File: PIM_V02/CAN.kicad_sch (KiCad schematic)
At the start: 40 parts, among them U4 MCP2562FDT-E/SN, U5 MCP2562FDT-E/SN

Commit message: more changes, near final schematic and part way through layout now
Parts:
- removed FL1, FL2: ACT45B-101-2P-TL003, CustomFootprints:ACT45B-101-2P-TL003_TDK, symbol Custom_Components:ACT45B-101-2P-TL003
- added FL1, FL2: Choke_CommonMode_FerriteCore_1243, Inductor_SMD:L_CommonModeChoke_Coilcraft_1812CAN, symbol Filter:Choke_CommonMode_FerriteCore_1243
- C10, C11, C14, C15: value C_Small -> 4.7uF
- C12, C13, C16, C17: value C_Small -> 0.1uF
- C18, C19, C20, C21, C22, C23, C24, C25: value C_Small -> 47pF
- C26, C27: value C_Small -> 4.7nF
- R14, R15: value R_Small -> 10kR
- R16, R17: value R_Small -> 0R
- R18, R19, R20, R21: value R_Small -> 60R
- R41, R42, R43, R44: value R_Small -> 1kR
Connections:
- net CAN0_N: now also FL1.2
- net CAN0_P: now also FL1.3
- net CAN0_RAW_N: now also FL1.1
- net CAN0_RAW_P: now also FL1.4
- net CAN1_N: now also FL2.2
- net CAN1_P: now also FL2.3
- net CAN1_RAW_N: now also FL2.1
- net CAN1_RAW_P: now also FL2.4
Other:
- note removed: "Common Mode Choke: - ACT1210L-101-2P-TL00 - If HF noise hits both lines in same dir, mag fields add together, creating high imepdance wall, suffocating noise"
- note removed: "PCHAN: LOGIC LEVEL 5V AO3401 or DMP2305"
- note removed: "READ THIS https://www.onsemi.com/download/application-notes/pdf/and90146-d.pdf"
- note removed: "TVS Diode: - VCAN16A2-03S-E3-08"
- note removed: "bus-line caps should be C0G/NP0 (X7R loses capacitance with applied voltage and is microphonic, so it distorts CAN edges nonlinearly)"
- note removed: "choke dot polarity??"
- note removed: "redundant can can high and low and gnd on 3 pin header AND HEADER"
- moved on the sheet: C10, C11, C12, C13, C14, C15, C16, C17, C18, C19, C20, C21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

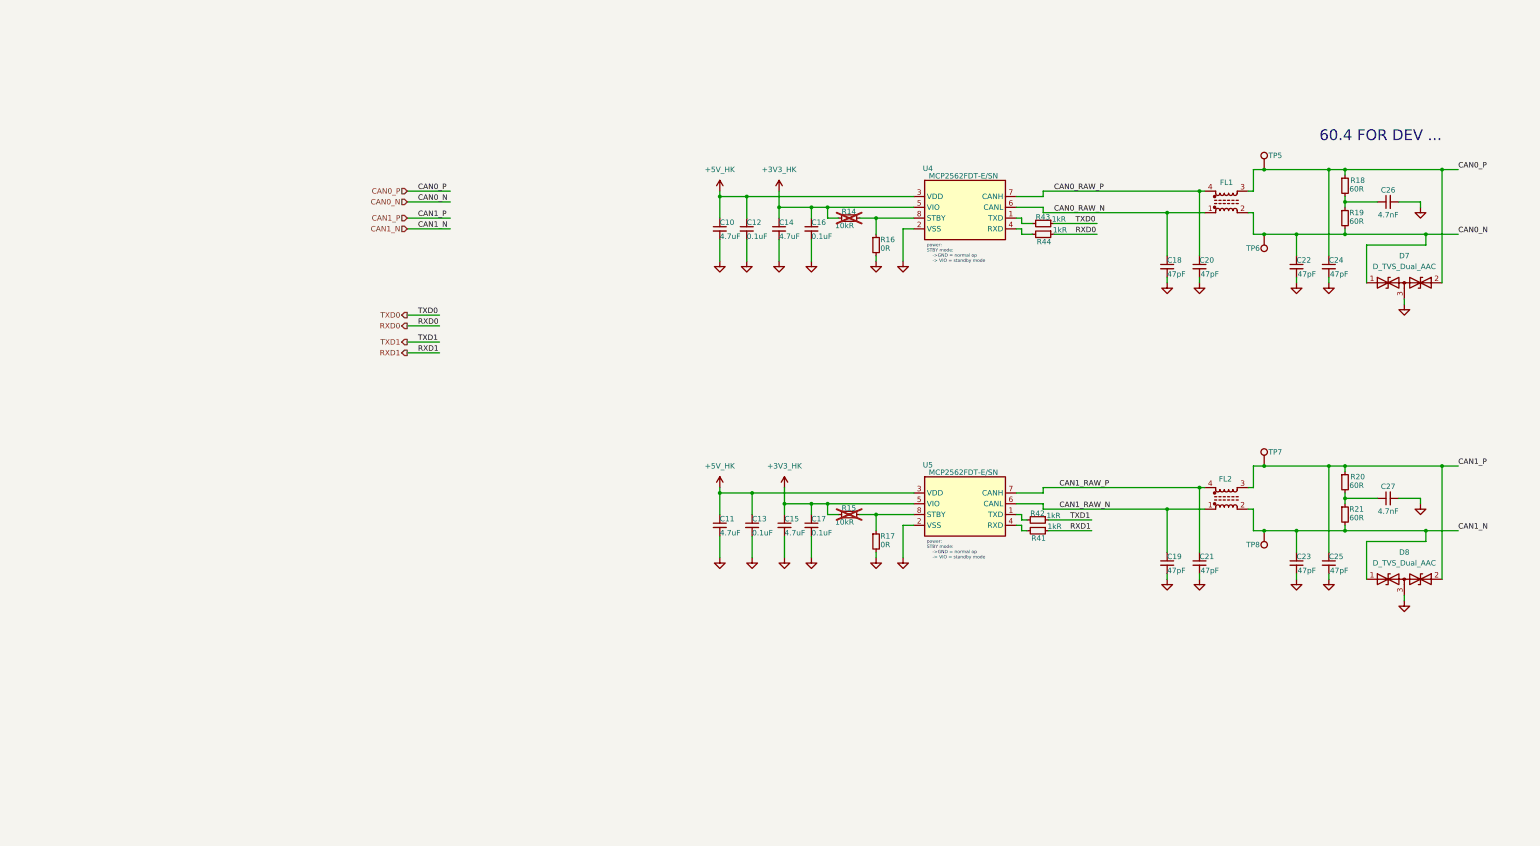
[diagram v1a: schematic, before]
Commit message: pc104 outline, nearly done with layout, managed to keep it at 4 layers but the traces became quite messy; still need to do an in depth review to ensure i havent cut across any zones unknowingly; also there are still DRC errors that i need to work through - but all nets are connected !
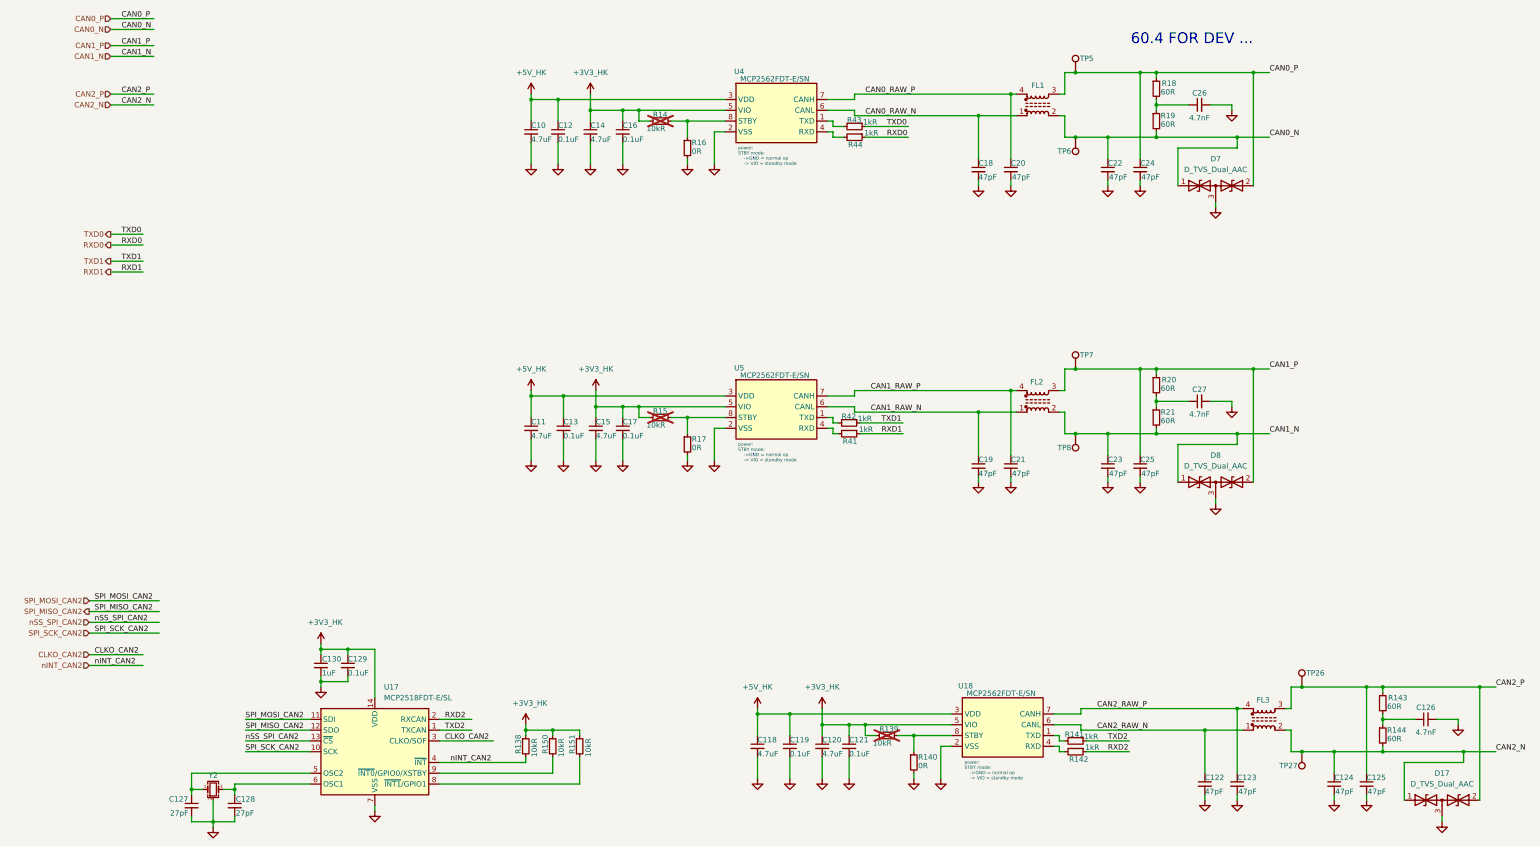
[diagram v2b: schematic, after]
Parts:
- added C118, C120: 4.7uF, Capacitor_SMD:C_0603_1608Metric, symbol Device:C_Small
- added C119, C121, C129: 0.1uF, Capacitor_SMD:C_0603_1608Metric, symbol Device:C_Small
- added C122, C123, C124, C125: 47pF, Capacitor_SMD:C_0603_1608Metric, symbol Device:C_Small
- added C126: 4.7nF, Capacitor_SMD:C_0603_1608Metric, symbol Device:C_Small
- added C127, C128: 27pF, Capacitor_SMD:C_0603_1608Metric, symbol Device:C_Small
- added C130: 1uF, Capacitor_SMD:C_0603_1608Metric, symbol Device:C_Small
- added D17: D_TVS_Dual_AAC, Package_TO_SOT_SMD:SOT-23-3, symbol Device:D_TVS_Dual_AAC
- added FL3: Choke_CommonMode_FerriteCore_1243, Inductor_SMD:L_CommonModeChoke_Coilcraft_1812CAN, symbol Filter:Choke_CommonMode_FerriteCore_1243
- added R138, R139, R150, R151: 10kR, Resistor_SMD:R_0603_1608Metric, symbol Device:R_Small
- added R140: 0R, Resistor_SMD:R_0603_1608Metric, symbol Device:R_Small
- added R141, R142: 1kR, Resistor_SMD:R_0603_1608Metric, symbol Device:R_Small
- added R143, R144: 60R, Resistor_SMD:R_0603_1608Metric, symbol Device:R_Small
- added TP26, TP27: TestPoint, TestPoint:TestPoint_Pad_D1.0mm, symbol Connector:TestPoint
- added U17: MCP2518FDT-E/SL, Package_SO:SOIC-14_3.9x8.7mm_P1.27mm, symbol Custom_Components:MCP2518FDT-E/SL
- added U18: MCP2562FDT-E/SN, Package_SO:SOIC-8_3.9x4.9mm_P1.27mm, symbol MyComponents:MCP2562FD-H/SN
- added Y2: Crystal_GND24_Small, Crystal:Crystal_SMD_Abracon_ABM8G-4Pin_3.2x2.5mm, symbol Device:Crystal_GND24_Small
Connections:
- net +3V3_HK: now also C120.1, C121.1, C129.1, C130.1, R138.1, R139.2, R150.1, R151.1, U17.14 (VDD), U18.5 (VIO)
- net +5V_HK: now also C118.1, C119.1, U18.3 (VDD)
- net GND: now also C118.2, C119.2, C120.2, C121.2, C122.2, C123.2, C124.2, C125.2, C126.2, C127.2, C128.2, C129.2, C130.2, D17.3 (common), R140.2, U17.15 (VSS), U17.7 (VSS), U18.2 (VSS), Y2.2 (G), Y2.4 (G)
- new net: R141.2, U18.1 (TXD)
- new net: R142.2, U18.4 (RXD)
- new net: R139.1, R140.1, U18.8 (STBY)
- new net: C126.1, R143.2, R144.1
- new net: C128.1, U17.6 (OSC1), Y2.3
- new net: C127.1, U17.5 (OSC2), Y2.1
- new net: R150.2, U17.9 (~{INT0}/GPIO0/XSTBY)
- new net: R151.2, U17.8 (~{INT1}/GPIO1)
- new net CAN2_N: C124.1, D17.1 (A1), FL3.2, R144.2, TP27.1
- new net CAN2_P: C125.1, D17.2 (A2), FL3.3, R143.1, TP26.1
- new net CAN2_RAW_N: C122.1, FL3.1, U18.6 (CANL)
- new net CAN2_RAW_P: C123.1, FL3.4, U18.7 (CANH)
- new net CLKO_CAN2: U17.3 (CLKO/SOF)
- new net RXD2: R142.1, U17.2 (RXCAN)
- new net SPI_MISO_CAN2: U17.12 (SDO)
- new net SPI_MOSI_CAN2: U17.11 (SDI)
- new net SPI_SCK_CAN2: U17.10 (SCK)
- new net TXD2: R141.1, U17.1 (TXCAN)
- new net nINT_CAN2: R138.2, U17.4 (~{INT})
- new net nSS_SPI_CAN2: U17.13 (~{CS})
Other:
- moved on the sheet: C10, C11, C12, C13, C14, C15, C16, C17, C18, C19, C20, C21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
